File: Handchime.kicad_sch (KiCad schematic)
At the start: 18 parts, among them J1 USB_C_Receptacle_USB2.0, J2 Pins, SW0 BOOT, SW1 Row 0, Col 0, SW2 Row 0, Col 1, U1 CH552T, U2 PRTR5V0U2X

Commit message: Rename from HandCHime to Handchime
With FAK development being discontinued, it no longer makes sense to use the **CH**552T. With an STM32, HandSTamp would make sense, but there are already a number of projects with “stamp”-based names. So the “Handchime” name stays, but without the emphasis on the “CH” part.
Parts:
- J2: footprint Project Library:HandCHime -> Project Library:Handchime; symbol Project Library:HandCHime -> Project Library:Handchime
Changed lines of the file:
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@@
 		)
 		(instances
-			(project "HandCHime"
+			(project "Handchime"
 				(path "/34400e51-cf83-464a-b3ec-e9a28a972a27"
 					(reference "C2")
@@
 		)
 		(instances
-			(project "HandCHime"
+			(project "Handchime"
 				(path "/34400e51-cf83-464a-b3ec-e9a28a972a27"
 					(reference "D3")
@@
 		)
 		(instances
-			(project "HandCHime"
+			(project "Handchime"
 				(path "/34400e51-cf83-464a-b3ec-e9a28a972a27"
 					(reference "#PWR08")
@@
 		)
 		(instances
-			(project "HandCHime"
+			(project "Handchime"
 				(path "/34400e51-cf83-464a-b3ec-e9a28a972a27"
 					(reference "SW2")
@@
 		)
 		(instances
-			(project "HandCHime"
+			(project "Handchime"
 				(path "/34400e51-cf83-464a-b3ec-e9a28a972a27"
 					(reference "R3")
@@
 		)
 		(instances
-			(project "HandCHime"
+			(project "Handchime"
 				(path "/34400e51-cf83-464a-b3ec-e9a28a972a27"
 					(reference "R1")
@@
 		)
 		(instances
-			(project "HandCHime"
+			(project "Handchime"
 				(path "/34400e51-cf83-464a-b3ec-e9a28a972a27"
 					(reference "#PWR09")
@@
 		)
 		(instances
-			(project "HandCHime"
+			(project "Handchime"
 				(path "/34400e51-cf83-464a-b3ec-e9a28a972a27"
 					(reference "#PWR020")
@@
 		)
 		(instances
-			(project "HandCHime"
+			(project "Handchime"
 				(path "/34400e51-cf83-464a-b3ec-e9a28a972a27"
 					(reference "#PWR011")
@@
 		)
 		(instances
-			(project "HandCHime"
+			(project "Handchime"
 				(path "/34400e51-cf83-464a-b3ec-e9a28a972a27"
 					(reference "U2")
@@
 		)
 		(instances
-			(project "HandCHime"
+			(project "Handchime"
 				(path "/34400e51-cf83-464a-b3ec-e9a28a972a27"
 					(reference "#PWR07")
@@
 		)
 		(instances
-			(project "HandCHime"
+			(project "Handchime"
 				(path "/34400e51-cf83-464a-b3ec-e9a28a972a27"
 					(reference "J1")
@@
 		)
 		(instances
-			(project "HandCHime"
+			(project "Handchime"
 				(path "/34400e51-cf83-464a-b3ec-e9a28a972a27"
 					(reference "#PWR01")
@@
 		)
 		(instances
-			(project "HandCHime"
+			(project "Handchime"
 				(path "/34400e51-cf83-464a-b3ec-e9a28a972a27"
 					(reference "#PWR017")
@@
 		)
 		(instances
-			(project "HandCHime"
+			(project "Handchime"
 				(path "/34400e51-cf83-464a-b3ec-e9a28a972a27"
 					(reference "#PWR016")
@@
 		)
 		(instances
-			(project "HandCHime"
+			(project "Handchime"
 				(path "/34400e51-cf83-464a-b3ec-e9a28a972a27"
 					(reference "#PWR021")
@@
 		)
 		(instances
-			(project "HandCHime"
+			(project "Handchime"
 				(path "/34400e51-cf83-464a-b3ec-e9a28a972a27"
 					(reference "#PWR05")
@@
 		)
 		(instances
-			(project "HandCHime"
+			(project "Handchime"
 				(path "/34400e51-cf83-464a-b3ec-e9a28a972a27"
 					(reference "#PWR018")
@@
 		)
 		(instances
-			(project "HandCHime"
+			(project "Handchime"
 				(path "/34400e51-cf83-464a-b3ec-e9a28a972a27"
 					(reference "D1")
@@
 		)
 		(instances
-			(project "HandCHime"
+			(project "Handchime"
 				(path "/34400e51-cf83-464a-b3ec-e9a28a972a27"
 					(reference "F1")
@@
 		)
 		(instances
-			(project "HandCHime"
+			(project "Handchime"
 				(path "/34400e51-cf83-464a-b3ec-e9a28a972a27"
 					(reference "D2")
@@
 		)
 		(instances
-			(project "HandCHime"
+			(project "Handchime"
 				(path "/34400e51-cf83-464a-b3ec-e9a28a972a27"
 					(reference "#PWR014")
@@
 		)
 		(instances
-			(project "HandCHime"
+			(project "Handchime"
 				(path "/34400e51-cf83-464a-b3ec-e9a28a972a27"
 					(reference "#PWR010")
@@
 		)
 		(instances
-			(project "HandCHime"
+			(project "Handchime"
 				(path "/34400e51-cf83-464a-b3ec-e9a28a972a27"
 					(reference "#PWR06")
@@
 		)
 		(instances
-			(project "HandCHime"
+			(project "Handchime"
 				(path "/34400e51-cf83-464a-b3ec-e9a28a972a27"
 					(reference "SW0")
@@
 		)
 		(instances
-			(project "HandCHime"
+			(project "Handchime"
 				(path "/34400e51-cf83-464a-b3ec-e9a28a972a27"
 					(reference "SW1")
@@
 		)
 		(instances
-			(project "HandCHime"
+			(project "Handchime"
 				(path "/34400e51-cf83-464a-b3ec-e9a28a972a27"
 					(reference "#PWR013")
@@
 		)
 		(instances
-			(project "HandCHime"
+			(project "Handchime"
 				(path "/34400e51-cf83-464a-b3ec-e9a28a972a27"
 					(reference "#PWR03")
@@
 		)
 		(instances
-			(project "HandCHime"
+			(project "Handchime"
 				(path "/34400e51-cf83-464a-b3ec-e9a28a972a27"
 					(reference "#PWR02")
@@
 		)
 		(instances
-			(project "HandCHime"
+			(project "Handchime"
 				(path "/34400e51-cf83-464a-b3ec-e9a28a972a27"
 					(reference "#PWR022")
@@
 		)
 		(instances
-			(project "HandCHime"
+			(project "Handchime"
 				(path "/34400e51-cf83-464a-b3ec-e9a28a972a27"
 					(reference "NT2")
@@
 		)
 		(instances
-			(project "HandCHime"
+			(project "Handchime"
 				(path "/34400e51-cf83-464a-b3ec-e9a28a972a27"
 					(reference "#PWR015")
@@
 	)
 	(symbol
-		(lib_id "Project Library:HandCHime")
+		(lib_id "Project Library:Handchime")
 		(at 204.47 139.7 0)
 		(unit 1)
@@
 			)
 		)
-		(property "Footprint" "Project Library:HandCHime"
+		(property "Footprint" "Project Library:Handchime"
 			(at 204.47 139.7 0)
 			(hide yes)
@@
 		)
 		(instances
-			(project "HandCHime"
+			(project "Handchime"
 				(path "/34400e51-cf83-464a-b3ec-e9a28a972a27"
 					(reference "J2")
@@
 		)
 		(instances
-			(project "HandCHime"
+			(project "Handchime"
 				(path "/34400e51-cf83-464a-b3ec-e9a28a972a27"
 					(reference "NT1")
@@
 		)
 		(instances
-			(project "HandCHime"
+			(project "Handchime"
 				(path "/34400e51-cf83-464a-b3ec-e9a28a972a27"
 					(reference "#PWR012")
@@
 		)
 		(instances
-			(project "HandCHime"
+			(project "Handchime"
 				(path "/34400e51-cf83-464a-b3ec-e9a28a972a27"
 					(reference "#PWR04")
@@
 		)
 		(instances
-			(project "HandCHime"
+			(project "Handchime"
 				(path "/34400e51-cf83-464a-b3ec-e9a28a972a27"
 					(reference "R2")
@@
 		)
 		(instances
-			(project "HandCHime"
+			(project "Handchime"
 				(path "/34400e51-cf83-464a-b3ec-e9a28a972a27"
 					(reference "#PWR023")
@@
 		)
 		(instances
-			(project "HandCHime"
+			(project "Handchime"
 				(path "/34400e51-cf83-464a-b3ec-e9a28a972a27"
 					(reference "#PWR019")
@@
 		)
 		(instances
-			(project "HandCHime"
+			(project "Handchime"
 				(path "/34400e51-cf83-464a-b3ec-e9a28a972a27"
 					(reference "U1")
@@
 		)
 		(instances
-			(project "HandCHime"
+			(project "Handchime"
 				(path "/34400e51-cf83-464a-b3ec-e9a28a972a27"
 					(reference "C1")

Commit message: Update schematic with STM32 version draft
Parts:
- removed C1, C2: 100nF, Capacitor_SMD:C_0603_1608Metric, symbol Device:C
- removed NT2: NetTie_2, Project Library:NetTie-2_SMD_Pad0.254mm, symbol Device:NetTie_2
- removed R3: 5.1k, Resistor_SMD:R_0603_1608Metric, symbol Device:R
- removed SW0: BOOT, Project Library:SW_SPST_B3U-1000P, symbol Switch:SW_Push
- removed U1: CH552T, Package_SO:TSSOP-20_4.4x6.5mm_P0.65mm, symbol Project Library:MCU_CH552T_TSSOP-20
- added C1, C2: 1µF, Capacitor_SMD:C_0603_1608Metric, symbol Device:C_Small
- added C3: 4.7µF, Capacitor_SMD:C_0603_1608Metric, symbol Device:C
- added C4, C5: 100nF, Capacitor_SMD:C_0603_1608Metric, symbol Device:C
- added J3: SWD, symbol Connector_Generic:Conn_01x01
- added J4: Clk, symbol Connector_Generic:Conn_01x01
- added R4: 10kΩ, Resistor_SMD:R_0603_1608Metric, symbol Device:R
- added R5: 330Ω, Resistor_SMD:R_0603_1608Metric, symbol Device:R
- added SW3: BOOT, Project Library:SW_SPST_B3U-1000P, symbol Switch:SW_Push
- added U3: STM32C071GBUx, Package_DFN_QFN:QFN-28_4x4mm_P0.5mm, symbol MCU_ST_STM32C0:STM32C071GBUx
- added U4: XC6206P332MR-G, Package_TO_SOT_SMD:SOT-23-3, symbol Regulator_Linear:XC6206PxxxMR
- J2: PIN10 10 -> B8; PIN11 11 -> A0; PIN12 13 -> (none); PIN13 33 -> A1; PIN14 (none) -> A2; PIN15 (none) -> A3; PIN16 30(TX) -> A4; PIN17 31(RX) -> A5; PIN19 (none) -> A6; PIN20 35 -> (none); PIN21 (none) -> A7; PIN22 (none) -> B0; PIN24 (none) -> B1; PIN3 14 -> B3; PIN5 15 -> B4; PIN6 16 -> B5; PIN7 17 -> (none); PIN8 (none) -> B6; PIN9 (none) -> B7
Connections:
- net P13 is gone; now on net C1: J2.12 (Col1)
- net P35 is gone; now on net GND: J2.20 (GND)
- net +3V3: now also J2.4 (3.3V), C2.1, C3.1, C4.1, SW3.2, U3.3 (VDD), U4.2 (VO); no longer J2.18 (3.3V)
- net C0: now also J2.18 (Col0), U3.16 (PA8); no longer J2.14 (Col0)
- net C1: now also U3.22 (PA15); no longer J2.9 (Col1)
- net GND: now also J2.25 (GND), J2.7 (GND), C1.2, C2.2, C3.2, C4.2, C5.2, R4.1, U3.4 (VSS), U4.1 (GND); no longer J2.15 (GND), J2.21 (GND), J2.8 (GND)
- net P17: no longer J2.7 (${PIN7})
- net R0: now also J2.26 (Row0), U3.17 (PC6); no longer J2.22 (Row0)
- net USB+: now also U3.19 (PA12)
- net USB-: now also U3.18 (PA11)
- net VCC: now also J2.23 (5V); no longer J2.19 (5V), J2.4 (5V)
- net GNDPWR renamed ISLAND
- net P10 renamed PB8
- net PB8: now also U3.28 (PB8)
- net P11 renamed PA0
- net PA0: now also U3.6 (PA0)
- net P14 renamed PB3
- net PB3: now also U3.23 (PB3)
- net P15 renamed PB4
- net PB4: now also U3.24 (PB4)
- net P16 renamed PB5
- net PB5: now also U3.25 (PB5)
- net P33 renamed PA1
- net PA1: now also U3.7 (PA1)
- net RX renamed PA5
- net PA5: now also U3.11 (PA5)
- net TX renamed PA4
- net PA4: now also U3.10 (PA4)
- new net: R5.2, SW3.1
- new net +5V: C1.1, U4.3 (VI)
- new net BOOT0/SWCLK: J4.1 (Pin_1), R4.2, R5.1, U3.21 (PA14)
- new net NRST: C5.1, U3.5 (PF2)
- new net PA2: J2.14 (${PIN14}), U3.8 (PA2)
- new net PA3: J2.15 (${PIN15}), U3.9 (PA3)
- new net PA6: J2.19 (${PIN19}), U3.12 (PA6)
- new net PA7: J2.21 (${PIN21}), U3.13 (PA7)
- new net PB0: J2.22 (${PIN22}), U3.14 (PB0)
- new net PB1: J2.24 (${PIN24}), U3.15 (PB1)
- new net PB6: J2.8 (${PIN8}), U3.26 (PB6)
- new net PB7: J2.9 (${PIN9}), U3.27 (PB7)
- new net SWDIO: J3.1 (Pin_1), U3.20 (PA13)
- no-connect marks 2 -> 4
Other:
- note added: "Power"
- moved on the sheet: NT1

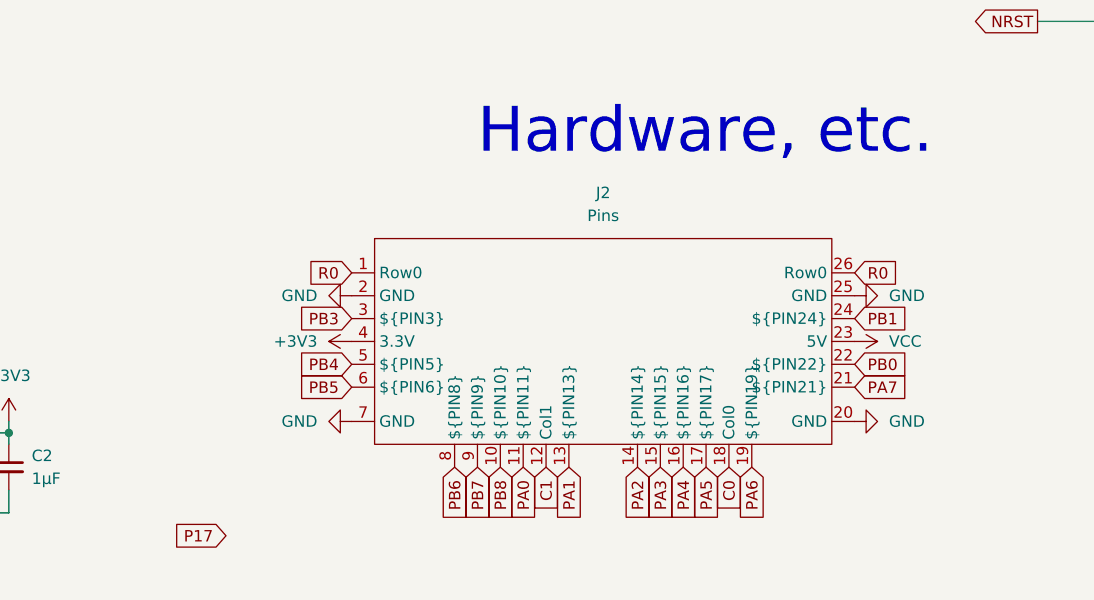
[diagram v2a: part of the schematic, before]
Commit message: Update breakout pin symbol and footprint
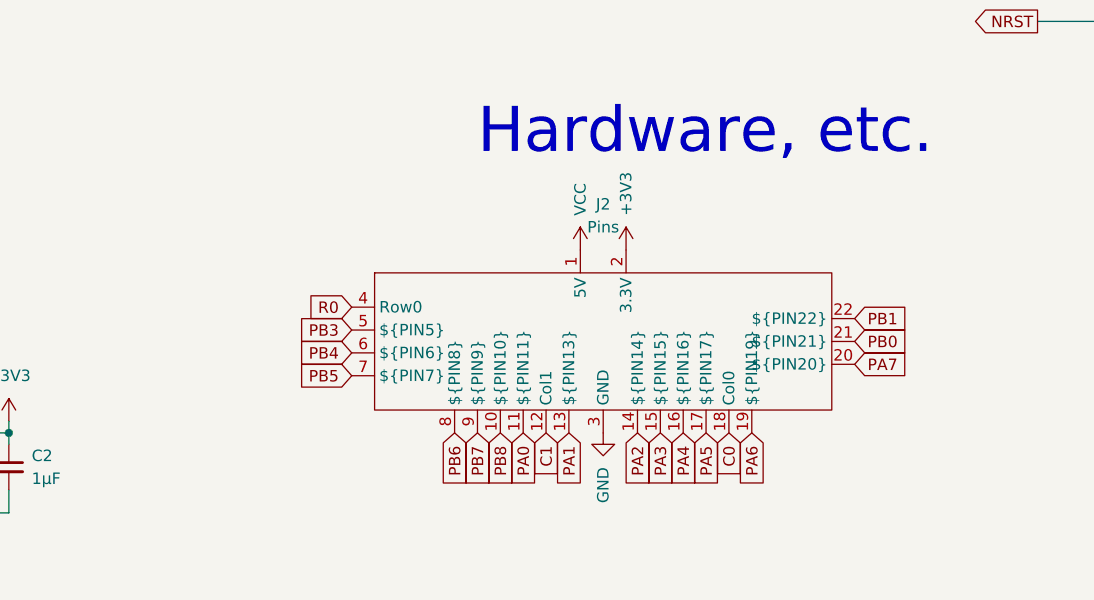
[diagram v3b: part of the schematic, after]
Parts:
- J2: PIN11 A0 -> A1; PIN13 A1 -> A2; PIN14 A2 -> A3; PIN15 A3 -> A4; PIN16 A4 -> A5; PIN17 A5 -> A6; PIN19 A6 -> A7; PIN20 (none) -> B0; PIN21 A7 -> B1; PIN22 B0 -> A0; PIN24 B1 -> (none); PIN3 B3 -> (none); PIN5 B4 -> B3; PIN6 B5 -> B4; PIN7 (none) -> B5
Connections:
- net +3V3: now also J2.2 (3.3V); no longer J2.4 (3.3V)
- net GND: now also J2.3 (GND); no longer J2.2 (GND), J2.20 (GND), J2.25 (GND), J2.7 (GND)
- net PA7: now also J2.20 (${PIN20}); no longer J2.21 (${PIN21})
- net PB0: now also J2.21 (${PIN21}); no longer J2.22 (${PIN22})
- net PB1: now also J2.22 (${PIN22}); no longer J2.24 (${PIN24})
- net PB3: now also J2.5 (${PIN5}); no longer J2.3 (${PIN3})
- net PB4: now also J2.6 (${PIN6}); no longer J2.5 (${PIN5})
- net PB5: now also J2.7 (${PIN7}); no longer J2.6 (${PIN6})
- net R0: now also J2.4 (Row0); no longer J2.1 (Row0), J2.26 (Row0)
- net VCC: now also J2.1 (5V); no longer J2.23 (5V)

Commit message: Update PCB with STH32 version draft
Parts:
- removed J1: USB_C_Receptacle_USB2.0, Connector_USB:USB_C_Receptacle_GCT_USB4105-xx-A_16P_TopMnt_Horizontal, symbol Connector:USB_C_Receptacle_USB2.0
- removed J4: Clk, symbol Connector_Generic:Conn_01x01
- added J1: USB_C_Receptacle_USB2.0_16P, Connector_USB:USB_C_Receptacle_HRO_TYPE-C-31-M-12, symbol Connector:USB_C_Receptacle_USB2.0_16P
- D1: footprint Project Library:D_SOD-323 -> BGK_Kicad:D_SOD-323
- J3: footprint (none) -> TestPoint:TestPoint_Pad_D1.0mm
- SW0: renamed from SW3; footprint Project Library:SW_SPST_B3U-1000P -> Button_Switch_SMD:SW_SPST_B3U-1000P
- renumbered U3 to U1, U4 to U3
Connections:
- net +5V is gone; now on net VCC: C1.1, U3.3 (VI)
- net +3V3: now also R5.2; no longer SW0.2
- net BOOT0/SWCLK: now also SW0.1; no longer R5.1
- net C1: now also U1.1 (PC14); no longer U1.22 (PA15)
- net ISLAND: now also J1.A1 (GND), J1.A12 (GND), J1.B1 (GND), J1.B12 (GND), J1.SH (SHIELD)
- net PA0: now also J2.13 (${PIN13}); no longer J2.11 (${PIN11})
- net PA1: now also J2.14 (${PIN14}); no longer J2.13 (${PIN13})
- net PA2: now also J2.15 (${PIN15}); no longer J2.14 (${PIN14})
- net PA3: now also J2.16 (${PIN16}); no longer J2.15 (${PIN15})
- net PA4: now also J2.17 (${PIN17}); no longer J2.16 (${PIN16})
- net PA5: now also J2.19 (${PIN19}); no longer J2.17 (${PIN17})
- net PA6: now also J2.20 (${PIN20}); no longer J2.19 (${PIN19})
- net PA7: now also J2.21 (${PIN21}); no longer J2.20 (${PIN20})
- net PB0: now also J2.22 (${PIN22}); no longer J2.21 (${PIN21})
- net PB3: now also J2.6 (${PIN6}); no longer J2.5 (${PIN5})
- net PB4: now also J2.7 (${PIN7}); no longer J2.6 (${PIN6})
- net PB5: now also J2.8 (${PIN8}); no longer J2.7 (${PIN7})
- net PB6: now also J2.9 (${PIN9}); no longer J2.8 (${PIN8})
- net PB7: now also J2.10 (${PIN10}); no longer J2.9 (${PIN9})
- net PB8: now also J2.11 (${PIN11}); no longer J2.10 (${PIN10})
- net R0: now also U1.15 (PB1); no longer U1.17 (PC6)
- net USB+: now also J1.A6 (D+), J1.B6 (D+)
- net USB-: now also J1.A7 (D-), J1.B7 (D-)
- net VBUS: now also J1.A4 (VBUS), J1.A9 (VBUS), J1.B4 (VBUS), J1.B9 (VBUS)
- net at R1.1: now also J1.A5 (CC1)
- net at R2.1: now also J1.B5 (CC2)
- removed net PB1: J2.22 (${PIN22}), U1.15 (PB1)
- new net: R5.1, SW0.2
- new net PA15: J2.5 (${PIN5}), U1.22 (PA15)
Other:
- moved on the sheet: R4

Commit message: Move components to work with relocated USB port
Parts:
- J3: footprint TestPoint:TestPoint_Pad_D1.0mm -> TestPoint:TestPoint_THTPad_D1.0mm_Drill0.5mm
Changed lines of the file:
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@@
 			)
 		)
-		(property "Footprint" "TestPoint:TestPoint_Pad_D1.0mm"
+		(property "Footprint" "TestPoint:TestPoint_THTPad_D1.0mm_Drill0.5mm"
 			(at 259.08 66.04 0)
 			(hide yes)

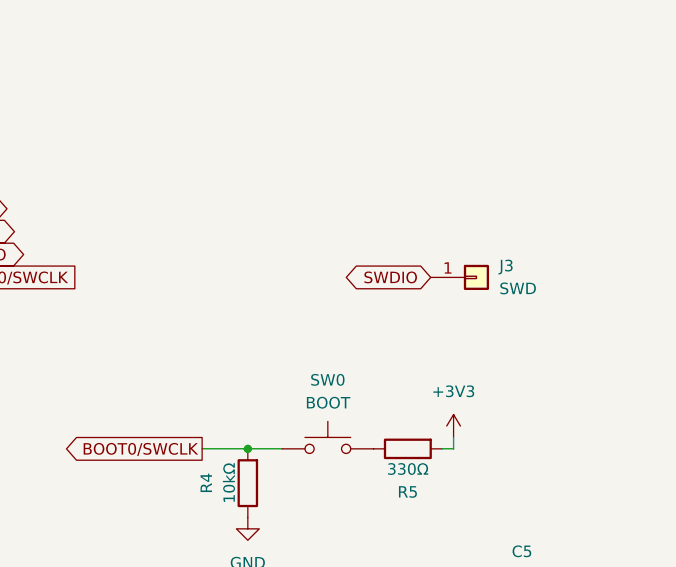
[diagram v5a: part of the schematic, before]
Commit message: Add 2-hole SWD access point
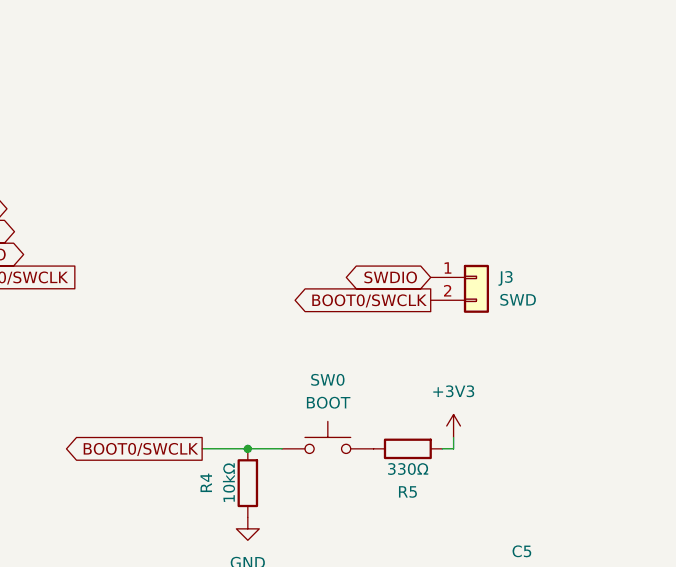
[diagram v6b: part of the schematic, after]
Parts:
- J3: footprint TestPoint:TestPoint_THTPad_D1.0mm_Drill0.5mm -> Connector_PinHeader_1.00mm:PinHeader_1x02_P1.00mm_Vertical; symbol Connector_Generic:Conn_01x01 -> Connector_Generic:Conn_01x02
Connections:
- net BOOT0/SWCLK: now also J3.2 (Pin_2)
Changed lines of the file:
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@@
+		)
+	)
+	(global_label "BOOT0{slash}SWCLK"
+		(shape output)
+		(at 254 68.58 180)
+		(fields_autoplaced yes)
+		(effects
+			(font
+				(size 1.27 1.27)
+			)
+			(justify right)
+		)
+		(property "Intersheetrefs" "${INTERSHEET_REFS}"
+			(at 239.5047 68.58 0)
+			(hide yes)
+			(show_name no)
+			(do_not_autoplace no)
+			(effects
+				(font
+					(size 1.27 1.27)
+				)
+				(justify right)
+			)
 		)
 	)
@@
 	)
 	(symbol
-		(lib_id "Connector_Generic:Conn_01x01")
+		(lib_id "Connector_Generic:Conn_01x02")
 		(at 259.08 66.04 0)
 		(unit 1)
@@
 		(fields_autoplaced yes)
 		(property "Reference" "J3"
-			(at 261.62 64.77 0)
+			(at 261.62 66.04 0)
 			(show_name no)
 			(do_not_autoplace no)
@@
 		)
 		(property "Value" "SWD"
-			(at 261.62 67.31 0)
+			(at 261.62 68.58 0)
 			(show_name no)
 			(do_not_autoplace no)
@@
 			)
 		)
-		(property "Footprint" "TestPoint:TestPoint_THTPad_D1.0mm_Drill0.5mm"
+		(property "Footprint" "Connector_PinHeader_1.00mm:PinHeader_1x02_P1.00mm_Vertical"
 			(at 259.08 66.04 0)
 			(hide yes)
@@
 			)
 		)
-		(property "Description" "Generic connector, single row, 01x01, script generated (kicad-library-utils/schlib/autogen/connector/)"
+		(property "Description" "Generic connector, single row, 01x02, script generated (kicad-library-utils/schlib/autogen/connector/)"
 			(at 259.08 66.04 0)
 			(hide yes)
@@
 		(pin "1"
 		)
+		(pin "2"
+		)
 		(instances
